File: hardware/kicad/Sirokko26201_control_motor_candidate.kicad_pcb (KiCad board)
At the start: 2 copper layers, 335 x 170 mm, 158 parts, among them J1 DEVKITC1_J1, J10 TC_K_EXHAUST_T+_T-, J102 MOTOR_24V_HIGH_SPEED; 125W_HE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, J11 TC_K_AIR_T+_T-, J12 ROOM_DS18B20_HARNESS, J13 24V_INPUT_PHOENIX_1756993_WIP, J22 START_STOP B3F-4055 + B32-138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, J23 ENCODER EC11E15244G1 + KNOB 4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, J24 RESET NKK BB25AB-FA, J26 TFT CABLE HARWIN M20-9960845 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, J27 GLOW_OUTPUT_PHOENIX_1756993, J28 CLUTCH_OUTPUT_PHOENIX_1756993, J3 DEVKITC1_J3, K1 DG85BM-5021-76-1024 + DZ85AB-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, K2 DG85BM-5021-76-1024 + DZ85AB-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, K3 DG85BM-5021-76-1024 + DZ85AB-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, Q1 IPB017N10N5LFATMA1 WIP, Q101 IRFB4110PBF (100V; RDS(on) @ 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, Q2 IPB017N10N5LFATMA1 WIP, Q20 BC847B,215, Q3 IPB017N10N5LFATMA1 WIP, Q4 IPB017N10N5LFATMA1 WIP, U1 TPS3431SDRBR, U10 MAX31856MUD+, U101 LM5013DDAR, U11 DRV8803PWPR, U13 LM74800QDRRRQ1 WIP_NOT_TRANSI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, U2 SN74HCS74D, U20 SN74LVC1G97DBVR, U301 TPS62162DSGR, U302 TPS3808G33DBVR, U303 74LVC125APW,118 Nexperia ONLY, U6 SN74HCS11D, U9 MAX31856MUD+, U9001 LTC7001IMSE#PBF; MSOP-10 EP, U9002 INA240A1ID, U9003 TLV9020DBVR, U9004 SN74LVC1G32DBVR, U9005 SN74LVC1G08DBVR, U9006 SN74LVC1G08DBVR, U9007 LM317HVT/NOPB TO-220; TJ 0…12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

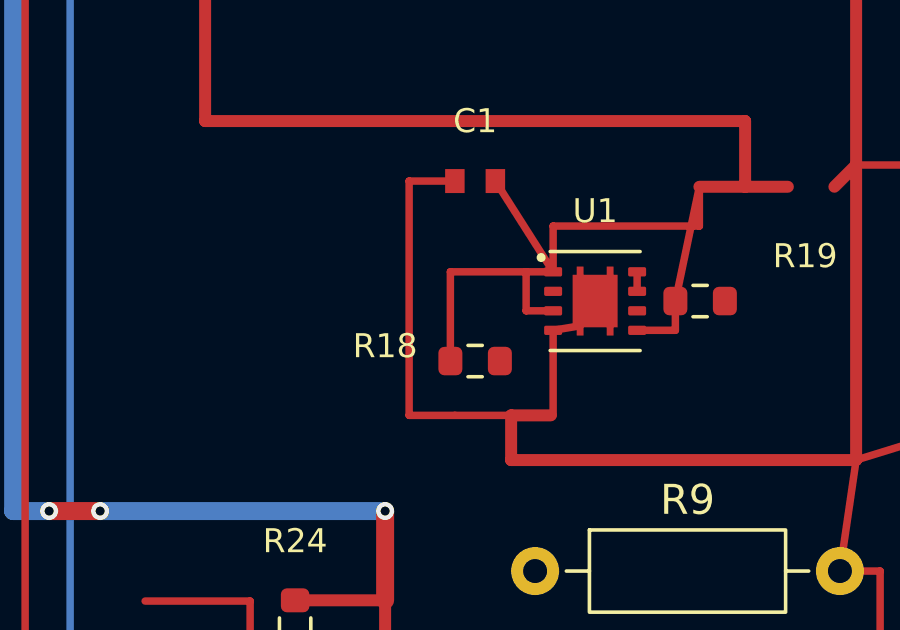
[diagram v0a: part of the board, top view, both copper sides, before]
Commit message: hardware: connect watchdog CWD signal
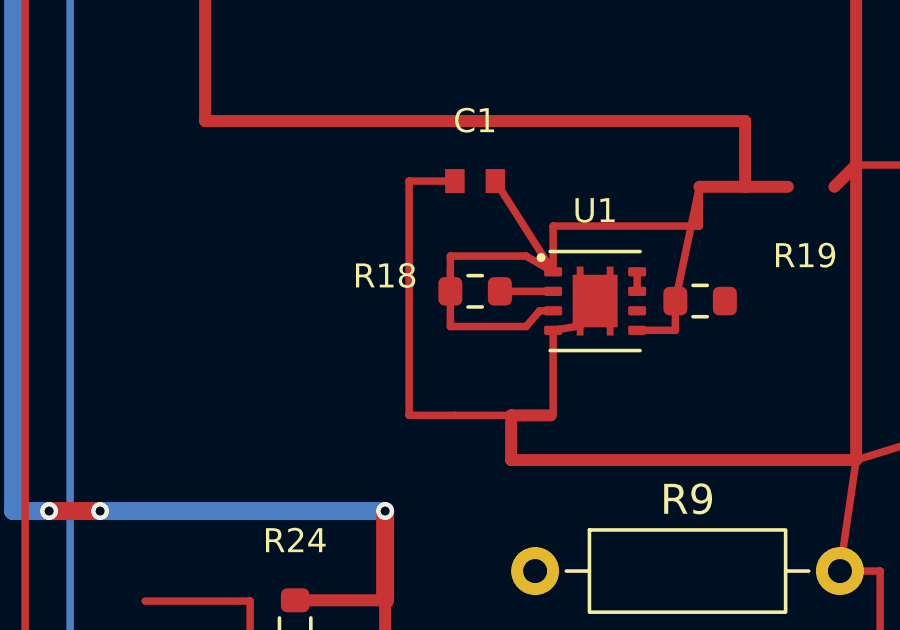
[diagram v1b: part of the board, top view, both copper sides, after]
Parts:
- moved R18 2.33 mm to (27.0, 64.7)
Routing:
- net /MinimalSafety/WD_CWD_FIXED: track 0.00 -> 1.78 mm
- net /+3V3: track 1318.3 -> 1319.2 mm
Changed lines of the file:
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@@
 	(footprint "Resistor_SMD:R_0603_1608Metric"
 		(layer "F.Cu")
-		(at 27 67)
+		(at 27 64.675)
 		(descr "Resistor SMD 0603 (1608 Metric), square (rectangular) end terminal, IPC-7351 nominal, (Body size source: IPC-SM-782 page 72, https://www.pcb-3d.com/wordpress/wp-content/uploads/ipc-sm-782a_amendment_1_and_2.pdf)")
 		(tags "resistor")
@@
 	)
 	(segment
-		(start 26.175 67)
-		(end 26.175 64.025)
-		(width 0.25)
-		(layer "F.Cu")
-		(net "/+3V3")
-	)
-	(segment
-		(start 29.6 64.025)
-		(end 28.7 64.025)
-		(width 0.25)
-		(layer "F.Cu")
-		(net "/+3V3")
-	)
-	(segment
 		(start 261.1375 173.05)
 		(end 261.1375 171.0875)
@@
 	)
 	(segment
-		(start 28.7 65.325)
-		(end 29.6 65.325)
-		(width 0.25)
-		(layer "F.Cu")
-		(net "/+3V3")
-	)
-	(segment
 		(start 165 110)
 		(end 167.8 110)
@@
 	)
 	(segment
-		(start 26.175 64.025)
-		(end 28.7 64.025)
-		(width 0.25)
-		(layer "F.Cu")
-		(net "/+3V3")
-	)
-	(segment
 		(start 49.475 61.19)
 		(end 49.825 58)
@@
 	)
 	(segment
-		(start 28.7 64.025)
-		(end 28.7 65.325)
-		(width 0.25)
-		(layer "F.Cu")
-		(net "/+3V3")
-	)
-	(segment
 		(start 125 105)
 		(end 128 105)
@@
 		(net "/EN_CHIP_PU")
 	)
+	(segment
+		(start 26.175 64.025)
+		(end 26.175 63.5)
+		(width 0.25)
+		(layer "F.Cu")
+		(net "/+3V3")
+	)
+	(segment
+		(start 26.175 63.5)
+		(end 28.7 63.5)
+		(width 0.25)
+		(layer "F.Cu")
+		(net "/+3V3")
+	)
+	(segment
+		(start 28.7 63.5)
+		(end 29.6 64.025)
+		(width 0.25)
+		(layer "F.Cu")
+		(net "/+3V3")
+	)
+	(segment
+		(start 29.6 65.325)
+		(end 29.15 65.325)
+		(width 0.25)
+		(layer "F.Cu")
+		(net "/+3V3")
+	)
+	(segment
+		(start 29.15 65.325)
+		(end 28.7 65.85)
+		(width 0.25)
+		(layer "F.Cu")
+		(net "/+3V3")
+	)
+	(segment
+		(start 28.7 65.85)
+		(end 26.175 65.85)
+		(width 0.25)
+		(layer "F.Cu")
+		(net "/+3V3")
+	)
+	(segment
+		(start 27.825 64.675)
+		(end 29.6 64.675)
+		(width 0.25)
+		(layer "F.Cu")
+		(net "/MinimalSafety/WD_CWD_FIXED")
+	)
+	(segment
+		(start 26.175 65.85)
+		(end 26.175 64.025)
+		(width 0.25)
+		(layer "F.Cu")
+		(net "/+3V3")
+	)
 	(zone

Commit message: hardware: finish watchdog WIP cleanup
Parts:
- moved R19 0.97 mm to (34.5, 64.0), turned to 180 degrees
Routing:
- net /+3V3: track 1319.2 -> 1320.8 mm
- net /MinimalSafety/WD_OK: track 1.92 -> 3.19 mm
- net /GND: vias 73 -> 72
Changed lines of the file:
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@@
 	(footprint "Resistor_SMD:R_0603_1608Metric"
 		(layer "F.Cu")
-		(at 34.5 65)
+		(at 34.5 64.025 180)
 		(descr "Resistor SMD 0603 (1608 Metric), square (rectangular) end terminal, IPC-7351 nominal, (Body size source: IPC-SM-782 page 72, https://www.pcb-3d.com/wordpress/wp-content/uploads/ipc-sm-782a_amendment_1_and_2.pdf)")
 		(tags "resistor")
 		(property "Reference" "R19"
-			(at 3.5 -1.5 0)
+			(at 0 -3.175 0)
 			(layer "F.SilkS")
 			(effects
@@
 		)
 		(property "Datasheet" "https://static.chipdip.ru/lib/175/DOC011175144.pdf"
-			(at 0 0 0)
+			(at 0 0 180)
 			(unlocked yes)
 			(layer "F.Fab")
@@
 		)
 		(property "Description" ""
-			(at 0 0 0)
+			(at 0 0 180)
 			(unlocked yes)
 			(layer "F.Fab")
@@
 		)
 		(property "MPN" "RC0603FR-0710KL"
-			(at 0 0 0)
+			(at 0 0 180)
 			(unlocked yes)
 			(layer "F.Fab")
@@
 		)
 		(property "Manufacturer" "YAGEO"
-			(at 0 0 0)
+			(at 0 0 180)
 			(unlocked yes)
 			(layer "F.Fab")
@@
 		)
 		(pad "1" smd roundrect
-			(at -0.825 0)
+			(at -0.825 0 180)
 			(size 0.8 0.95)
 			(layers "F.Cu" "F.Mask" "F.Paste")
@@
 		)
 		(pad "2" smd roundrect
-			(at 0.825 0)
+			(at 0.825 0 180)
 			(size 0.8 0.95)
 			(layers "F.Cu" "F.Mask" "F.Paste")
@@
 	)
 	(segment
-		(start 33.675 65)
-		(end 34.475 61.19)
-		(width 0.25)
-		(layer "F.Cu")
-		(net "/+3V3")
-	)
-	(segment
 		(start 165 105)
 		(end 165 107.5)
@@
 	)
 	(segment
-		(start 33.675 65.975)
-		(end 32.4 65.975)
-		(width 0.25)
-		(layer "F.Cu")
-		(net "/+3V3")
-	)
-	(segment
 		(start 270.5 156.635)
 		(end 272.475 156.635)
@@
 	)
 	(segment
-		(start 34.475 62.5)
-		(end 34.475 61.19)
-		(width 0.25)
-		(layer "F.Cu")
-		(net "/+3V3")
-	)
-	(segment
 		(start 62.8 98)
 		(end 65.175 98)
@@
 	)
 	(segment
-		(start 33.675 65)
-		(end 33.675 65.975)
-		(width 0.25)
-		(layer "F.Cu")
-		(net "/+3V3")
-	)
-	(segment
 		(start 62.5 36.5)
 		(end 73.225 36.5)
@@
 	)
 	(via
-		(at 83 26)
-		(size 0.6)
-		(drill 0.3)
-		(layers "F.Cu" "B.Cu")
-		(net "/GND")
-	)
-	(via
 		(at 177.6 138.05)
 		(size 0.6)
@@
 		(net "/+3V3")
 	)
+	(segment
+		(start 34.475 62.5)
+		(end 34.475 61.19)
+		(width 0.25)
+		(layer "F.Cu")
+		(net "/+3V3")
+	)
+	(segment
+		(start 32.4 65.975)
+		(end 35.325 65.975)
+		(width 0.25)
+		(layer "F.Cu")
+		(net "/+3V3")
+	)
+	(segment
+		(start 35.325 65.975)
+		(end 35.325 61.19)
+		(width 0.25)
+		(layer "F.Cu")
+		(net "/+3V3")
+	)
+	(segment
+		(start 32.4 64.025)
+		(end 33.675 64.025)
+		(width 0.25)
+		(layer "F.Cu")
+		(net "/MinimalSafety/WD_OK")
+	)
 	(zone

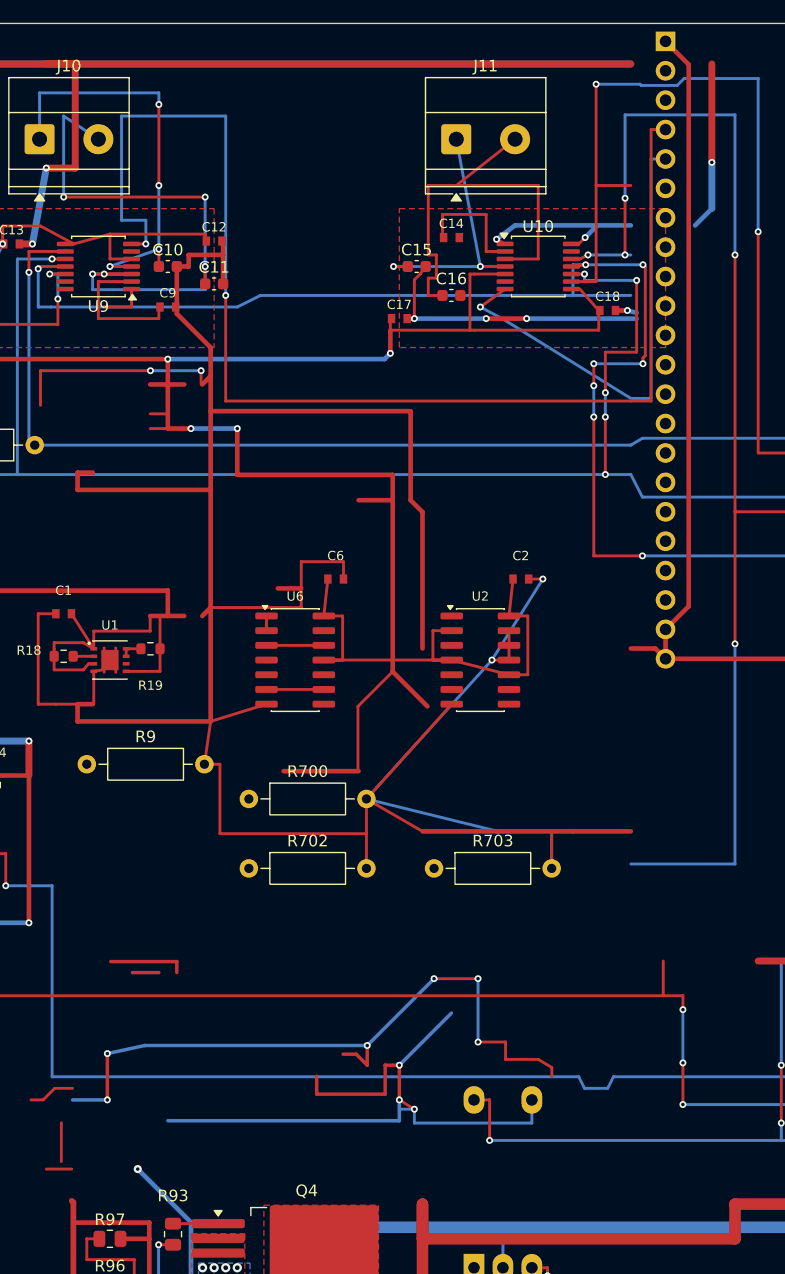
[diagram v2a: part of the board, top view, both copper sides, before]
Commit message: hardware: verify WD_OK and close two GND gaps
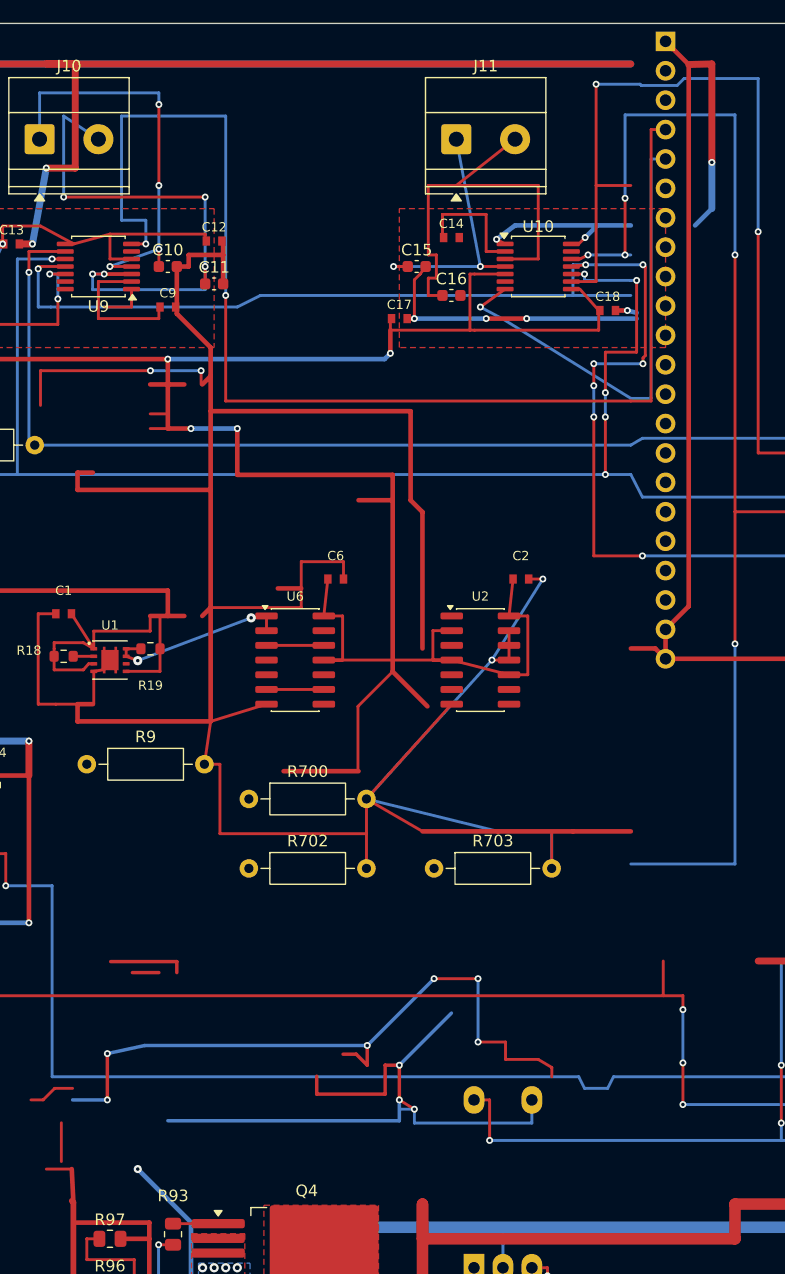
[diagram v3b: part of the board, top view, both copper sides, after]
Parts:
- C105, C106: value 47uF 16V X7R -> 47uF 16V X5R
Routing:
- net /MinimalSafety/WD_OK: track 3.19 -> 16.1 mm, vias 0 -> 2
- net /GND: track 2207.9 -> 2212.8 mm
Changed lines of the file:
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@@
 			)
 		)
-		(property "Value" "47uF 16V X7R"
+		(property "Value" "47uF 16V X5R"
 			(at 0 2.3 90)
 			(layer "F.Fab")
@@
 			)
 		)
-		(property "Value" "47uF 16V X7R"
+		(property "Value" "47uF 16V X5R"
 			(at 0 2.3 90)
 			(layer "F.Fab")
@@
 		(duplicate_pad_numbers_are_jumpers no)
 		(fp_line
-			(start -0.237258 -0.5225)
-			(end 0.237258 -0.5225)
+			(start -0.237258 0.5225)
+			(end 0.237258 0.5225)
 			(stroke
 				(width 0.12)
@@
 		)
 		(fp_line
-			(start -0.237258 0.5225)
-			(end 0.237258 0.5225)
+			(start -0.237258 -0.5225)
+			(end 0.237258 -0.5225)
 			(stroke
 				(width 0.12)
@@
 	)
 	(segment
+		(start 29.15 65.325)
+		(end 28.7 65.85)
+		(width 0.25)
+		(layer "F.Cu")
+		(net "/+3V3")
+	)
+	(segment
 		(start 32.125 30.35)
 		(end 31 30.35)
@@
 	)
 	(segment
+		(start 35.325 65.975)
+		(end 35.325 61.19)
+		(width 0.25)
+		(layer "F.Cu")
+		(net "/+3V3")
+	)
+	(segment
 		(start 65.175 99.5)
 		(end 68 99.5)
@@
 	)
 	(segment
+		(start 32.4 65.975)
+		(end 35.325 65.975)
+		(width 0.25)
+		(layer "F.Cu")
+		(net "/+3V3")
+	)
+	(segment
 		(start 18 42.77)
 		(end 18 39)
@@
 	)
 	(segment
+		(start 28.7 63.5)
+		(end 29.6 64.025)
+		(width 0.25)
+		(layer "F.Cu")
+		(net "/+3V3")
+	)
+	(segment
 		(start 18 46.43)
 		(end 18 42.77)
@@
 	)
 	(segment
+		(start 26.175 64.025)
+		(end 26.175 63.5)
+		(width 0.25)
+		(layer "F.Cu")
+		(net "/+3V3")
+	)
+	(segment
 		(start 128 107.5)
 		(end 145 107.5)
@@
 	)
 	(segment
+		(start 26.175 65.85)
+		(end 26.175 64.025)
+		(width 0.25)
+		(layer "F.Cu")
+		(net "/+3V3")
+	)
+	(segment
 		(start 145 107.5)
 		(end 145 110)
@@
 	)
 	(segment
+		(start 29.6 65.325)
+		(end 29.15 65.325)
+		(width 0.25)
+		(layer "F.Cu")
+		(net "/+3V3")
+	)
+	(segment
 		(start 55.225 38.5)
 		(end 55.225 36.5)
@@
 	)
 	(segment
+		(start 34.475 62.5)
+		(end 34.475 61.19)
+		(width 0.25)
+		(layer "F.Cu")
+		(net "/+3V3")
+	)
+	(segment
 		(start 55.425 66)
 		(end 58.425 69)
@@
 	)
 	(segment
+		(start 28.7 65.85)
+		(end 26.175 65.85)
+		(width 0.25)
+		(layer "F.Cu")
+		(net "/+3V3")
+	)
+	(segment
 		(start 71.6 32.95)
 		(end 73.225 34.8)
@@
 	)
 	(segment
+		(start 26.175 63.5)
+		(end 28.7 63.5)
+		(width 0.25)
+		(layer "F.Cu")
+		(net "/+3V3")
+	)
+	(segment
 		(start 67.1 61.19)
 		(end 67.1 66.27)
@@
 	)
 	(segment
+		(start 27.825 64.675)
+		(end 29.6 64.675)
+		(width 0.25)
+		(layer "F.Cu")
+		(net "/MinimalSafety/WD_CWD_FIXED")
+	)
+	(segment
 		(start 156.4625 146)
 		(end 158.35 146)
@@
 	)
 	(segment
+		(start 83 13.5)
+		(end 81 13.55)
+		(width 0.6)
+		(layer "F.Cu")
+		(net "/GND")
+	)
+	(segment
 		(start 121.975 52.5)
 		(end 123.5 52.5)
@@
 	)
 	(segment
+		(start 27.7 108.975)
+		(end 27.84 111.86)
+		(width 0.4)
+		(layer "F.Cu")
+		(net "/GND")
+	)
+	(segment
 		(start 152.5 150.7)
 		(end 155.95 150.7)
@@
 	)
 	(segment
+		(start 43.2 61.35)
+		(end 44.525 61.19)
+		(width 0.25)
+		(layer "F.Cu")
+		(net "/MinimalSafety/WD_OK")
+	)
+	(segment
+		(start 32.4 64.025)
+		(end 33.675 64.025)
+		(width 0.25)
+		(layer "F.Cu")
+		(net "/MinimalSafety/WD_OK")
+	)
+	(segment
+		(start 32.4 64.675)
+		(end 33.4 65.05)
+		(width 0.25)
+		(layer "F.Cu")
+		(net "/MinimalSafety/WD_OK")
+	)
+	(segment
 		(start 32.4 64.025)
 		(end 32.4 64.675)
@@
 		(net "/MinimalSafety/WD_OK")
 	)
+	(via
+		(at 43.2 61.35)
+		(size 0.8)
+		(drill 0.3)
+		(layers "F.Cu" "B.Cu")
+		(net "/MinimalSafety/WD_OK")
+	)
+	(via
+		(at 33.4 65.05)
+		(size 0.8)
+		(drill 0.3)
+		(layers "F.Cu" "B.Cu")
+		(net "/MinimalSafety/WD_OK")
+	)
+	(segment
+		(start 33.4 65.05)
+		(end 43.2 61.35)
+		(width 0.25)
+		(layer "B.Cu")
+		(net "/MinimalSafety/WD_OK")
+	)
 	(segment
 		(start 264.675 168)
@@
 		(net "/EN_CHIP_PU")
 	)
-	(segment
-		(start 26.175 64.025)
-		(end 26.175 63.5)
-		(width 0.25)
-		(layer "F.Cu")
-		(net "/+3V3")
-	)
-	(segment
-		(start 26.175 63.5)
-		(end 28.7 63.5)
-		(width 0.25)
-		(layer "F.Cu")
-		(net "/+3V3")
-	)
-	(segment
-		(start 28.7 63.5)
-		(end 29.6 64.025)
-		(width 0.25)
-		(layer "F.Cu")
-		(net "/+3V3")
-	)
-	(segment
-		(start 29.6 65.325)
-		(end 29.15 65.325)
-		(width 0.25)
-		(layer "F.Cu")
-		(net "/+3V3")
-	)
-	(segment
-		(start 29.15 65.325)
-		(end 28.7 65.85)
-		(width 0.25)
-		(layer "F.Cu")
-		(net "/+3V3")
-	)
-	(segment
-		(start 28.7 65.85)
-		(end 26.175 65.85)
-		(width 0.25)
-		(layer "F.Cu")
-		(net "/+3V3")
-	)
-	(segment
-		(start 27.825 64.675)
-		(end 29.6 64.675)
-		(width 0.25)
-		(layer "F.Cu")
-		(net "/MinimalSafety/WD_CWD_FIXED")
-	)
-	(segment
-		(start 26.175 65.85)
-		(end 26.175 64.025)
-		(width 0.25)
-		(layer "F.Cu")
-		(net "/+3V3")
-	)
-	(segment
-		(start 34.475 62.5)
-		(end 34.475 61.19)
-		(width 0.25)
-		(layer "F.Cu")
-		(net "/+3V3")
-	)
-	(segment
-		(start 32.4 65.975)
-		(end 35.325 65.975)
-		(width 0.25)
-		(layer "F.Cu")
-		(net "/+3V3")
-	)
-	(segment
-		(start 35.325 65.975)
-		(end 35.325 61.19)
-		(width 0.25)
-		(layer "F.Cu")
-		(net "/+3V3")
-	)
-	(segment
-		(start 32.4 64.025)
-		(end 33.675 64.025)
-		(width 0.25)
-		(layer "F.Cu")
-		(net "/MinimalSafety/WD_OK")
-	)
 	(zone
